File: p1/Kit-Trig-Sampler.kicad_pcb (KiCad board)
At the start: 2 copper layers, 78 x 109.2 mm, 85 parts, among them J1 START_CV, J10 AUDIO_INR, J11 AUDIO_OUTL, J13 BANK_CV, J14 Eurorack_Power_16pin_Unshroud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, J2 LENGTH_CV, J3 SAMP_CV, J4 PITCH CV, J5 REV_TRIG, J6 PLAY_TRIG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

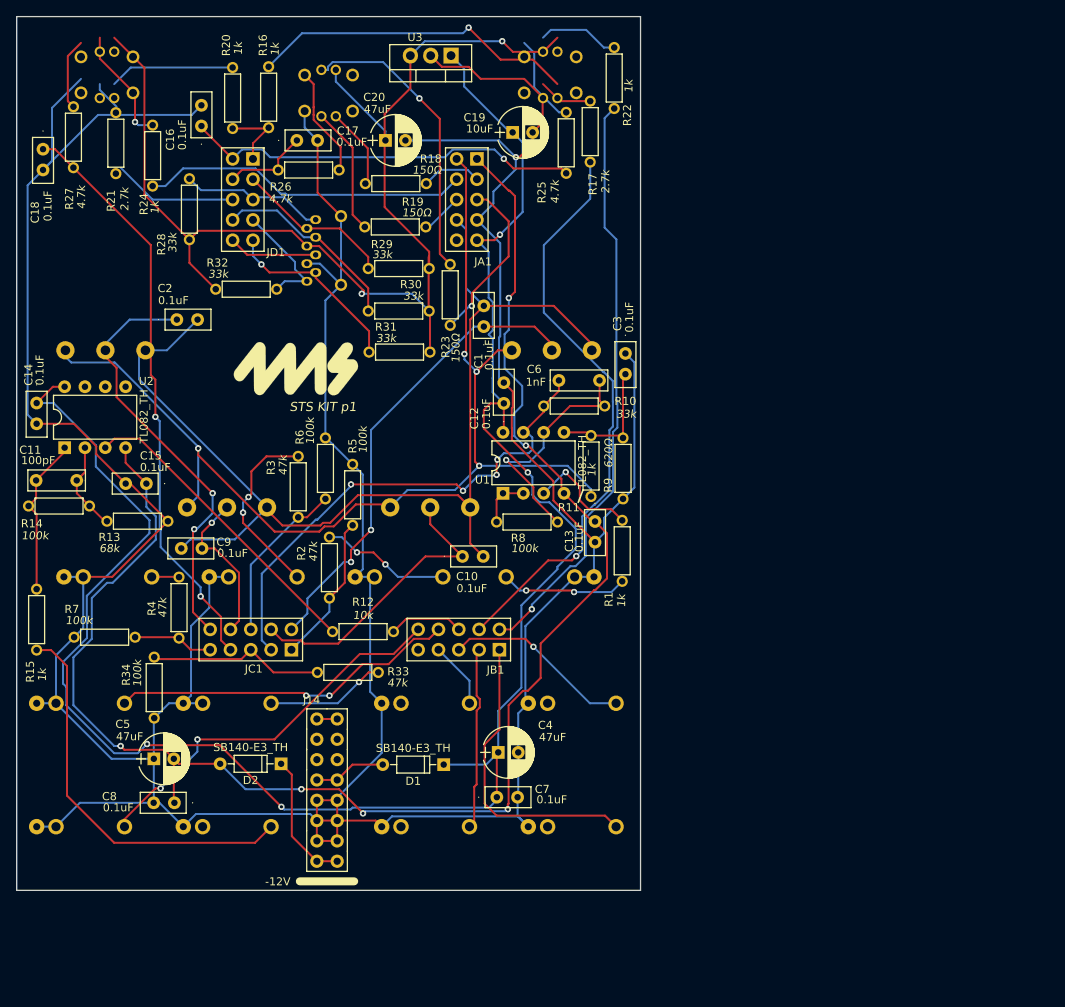
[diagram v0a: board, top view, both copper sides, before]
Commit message: nudged some parts for to match DLD layout
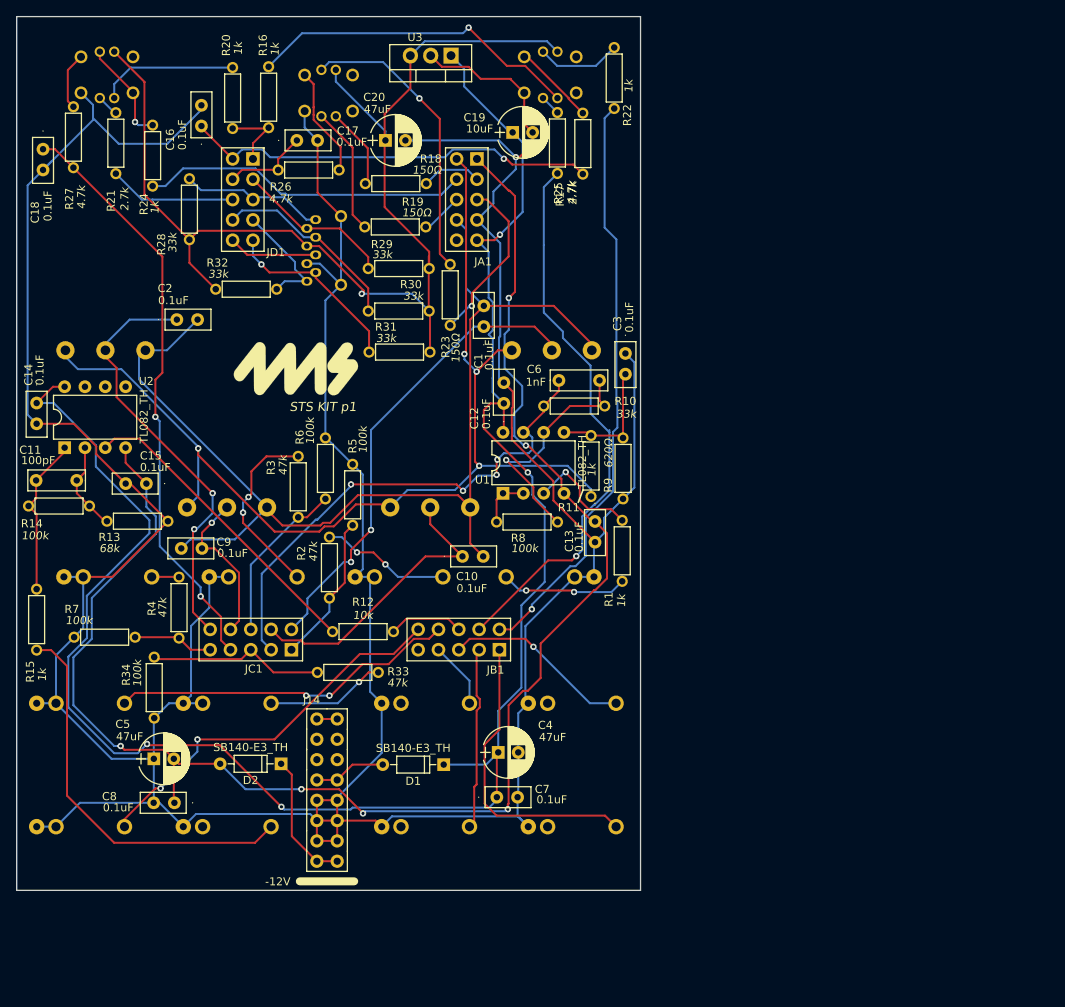
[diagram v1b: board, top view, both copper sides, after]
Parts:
- moved R17 4.34 mm to (28.6, 15.7)
- moved R25 2.08 mm to (31.8, 15.8)
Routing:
- net GND: track 524.5 -> 517.6 mm
- net +12V: track 238.8 -> 234.3 mm
- net Net-(Bank_But1-Pad7): track 6.78 -> 2.55 mm
- net /D1: track 73.2 -> 69.9 mm
- net +3V3: track 147.5 -> 145.0 mm, vias 2 -> 1
- net /D6: track 49.7 -> 51.8 mm
- net Net-(R27-Pad1): track 8.95 -> 7.20 mm
- net Net-(R20-Pad2): track 15.7 -> 17.4 mm
- net Net-(R24-Pad1): track 14.7 -> 13.0 mm
- net Net-(Bank_But1-Pad2): track 11.4 -> 10.3 mm
- net Net-(R21-Pad2): track 3.70 -> 2.69 mm
- net /A6: track 73.1 -> 73.9 mm
- net Net-(Bank_But1-Pad8): track 41.0 -> 41.8 mm

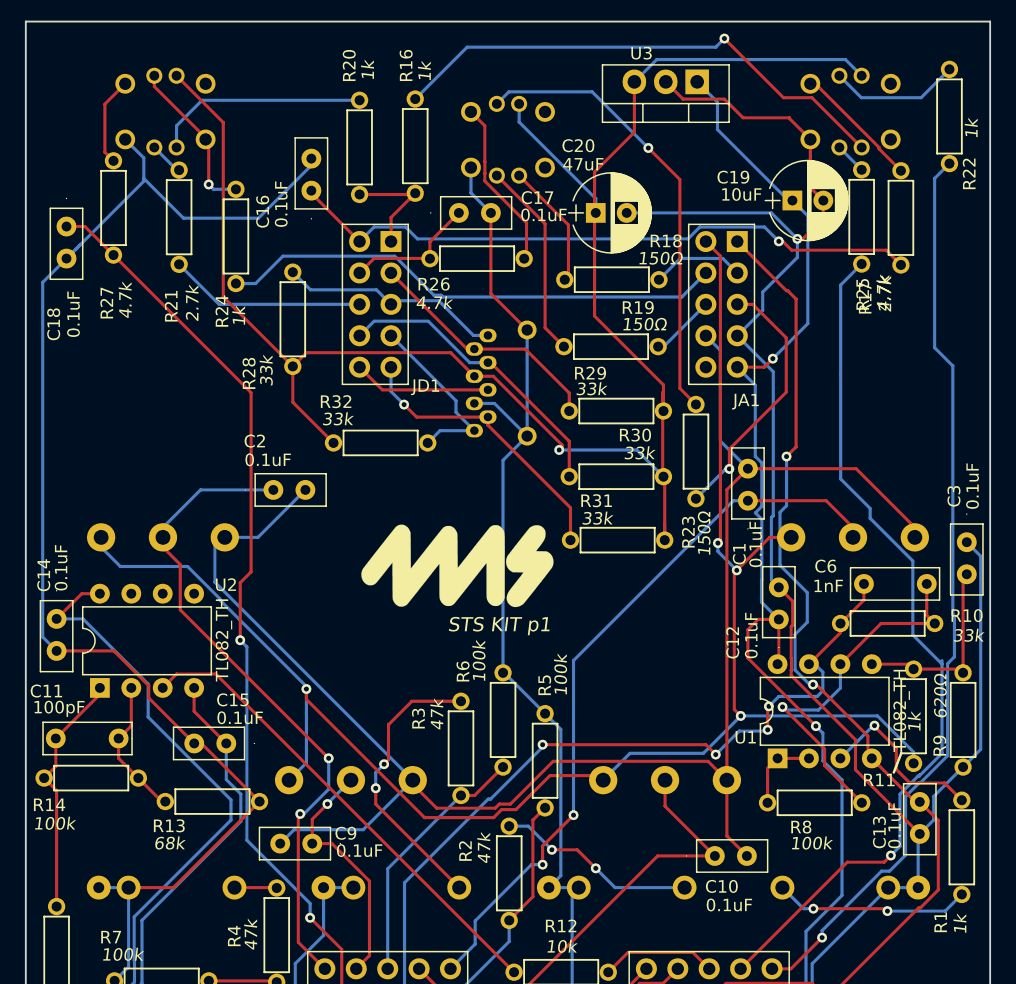
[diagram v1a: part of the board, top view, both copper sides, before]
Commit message: small update to silk
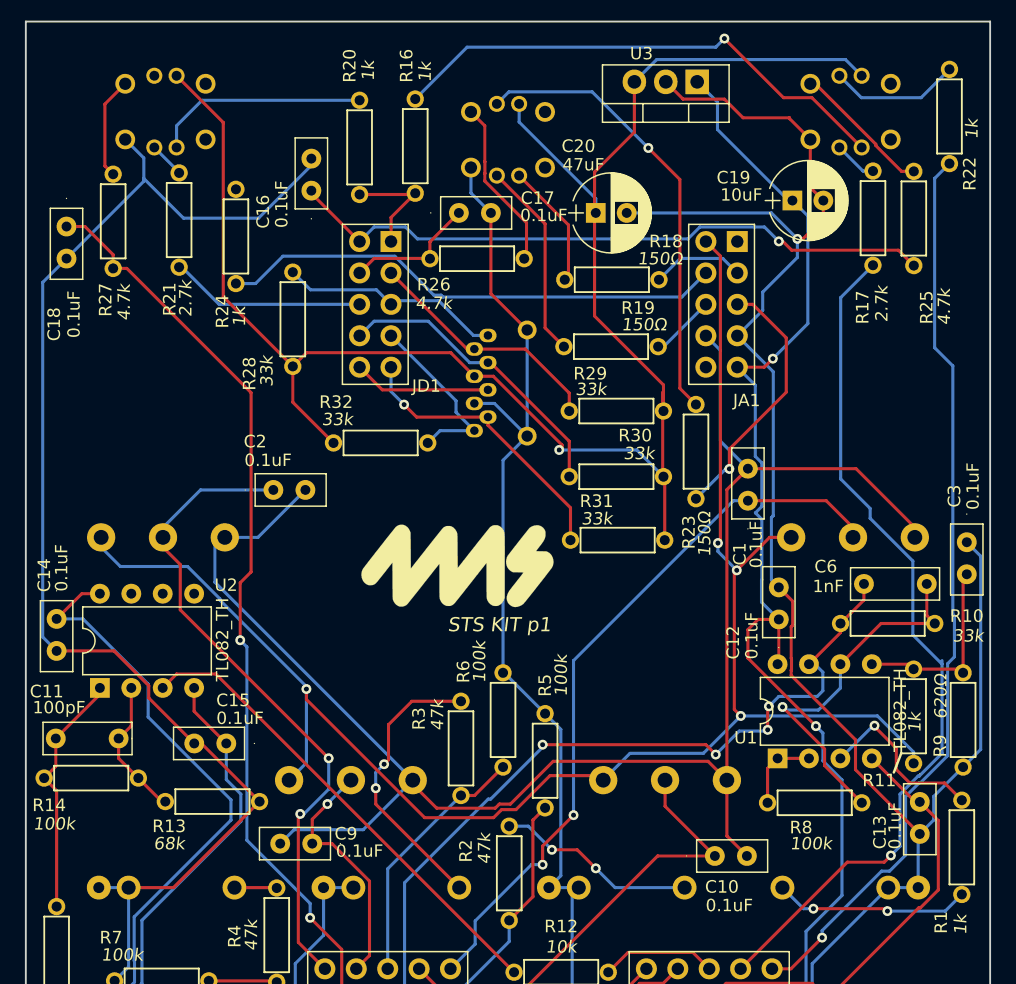
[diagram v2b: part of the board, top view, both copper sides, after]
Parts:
- moved R27 1.08 mm to (-31.9, 16.1)
- moved R25 1.04 mm to (32.8, 15.8)
- moved R17 0.92 mm to (29.5, 15.8)
- moved R21 0.23 mm to (-26.6, 16.0)
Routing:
- net -12VA: track 198.4 -> 150.7 mm, vias 6 -> 4
- net Net-(R24-Pad1): track 13.0 -> 0.00 mm, vias 1 -> 0
- net GND: track 517.6 -> 515.5 mm
- net +3V3: track 145.0 -> 143.2 mm
- net Net-(R27-Pad1): track 7.20 -> 8.27 mm
- net /D6: track 51.8 -> 52.9 mm
- net Net-(Bank_But1-Pad7): track 2.55 -> 3.50 mm
- net Net-(Bank_But1-Pad2): track 10.3 -> 11.0 mm
- net /A6: track 73.9 -> 74.5 mm

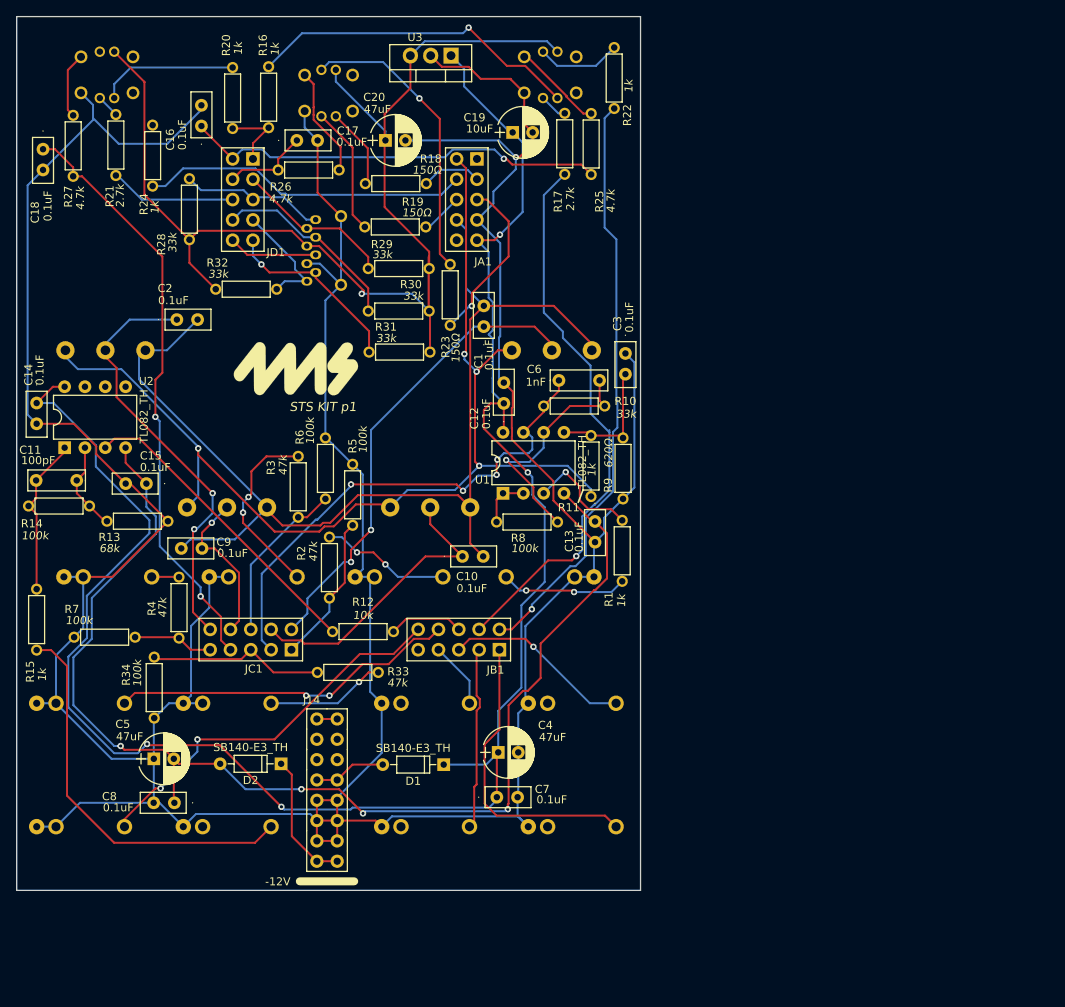
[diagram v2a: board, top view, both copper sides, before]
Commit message: updates to part placement
so it matches the faceplate
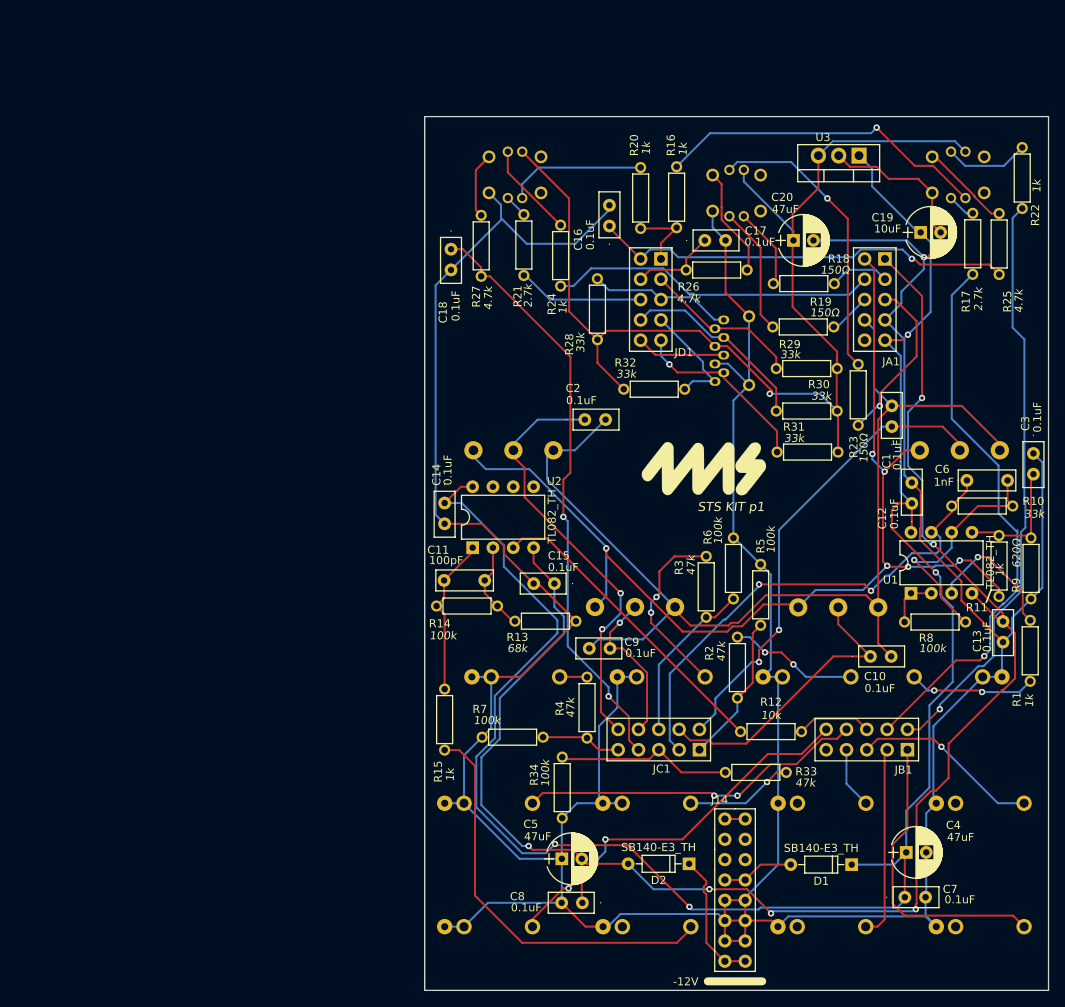
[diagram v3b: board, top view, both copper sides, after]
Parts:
- moved J7 53.9 mm to (40.1, 113.7)
- moved J13 53.9 mm to (40.0, 98.3)
- moved SD1 52.5 mm to (51.0, 41.3)
- moved POT_PITCH1 52.5 mm to (78.9, 41.2)
- moved Bank_But1 52.5 mm to (78.7, 19.7)
- moved C11 52.5 mm to (17.0, 70.4)
- moved C13 52.5 mm to (84.3, 76.8)
- moved C14 52.5 mm to (14.5, 62.0)
- moved C15 52.5 mm to (26.9, 70.8)
- moved C16 52.5 mm to (35.1, 24.8)
- moved C18 52.5 mm to (15.3, 30.3)
- moved C2 52.5 mm to (33.3, 50.3)
- moved C4 52.5 mm to (72.2, 104.4)
- moved C5 52.5 mm to (29.1, 105.2)
- moved C6 52.5 mm to (82.3, 57.9)
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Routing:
- net -12VA: track 150.7 -> 203.8 mm, vias 4 -> 6
- net Net-(R24-Pad1): track 0.00 -> 11.9 mm
- net Net-(R1-Pad2): track 14.5 -> 17.2 mm
- net /AUDIO_OUT1: track 21.7 -> 23.6 mm
- net Net-(J7-Pad1): track 49.6 -> 51.2 mm
- net Net-(J13-Pad1): track 15.0 -> 13.6 mm
- net /A2: track 62.9 -> 61.8 mm, vias 4 -> 2
- net VREF+: track 136.0 -> 136.7 mm, vias 4 -> 6
- net /AUDIO_IN1: track 8.30 -> 7.70 mm
